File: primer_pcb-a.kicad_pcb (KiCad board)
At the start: 2 copper layers, 50 x 50 mm, 4 parts, among them J1 Pinheader - muški, J2 Pinheader - ženski, J3 Pinheader - ženski, J4 Pinheader - muški

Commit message: ds
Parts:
- added J5: Pinheader - ženski, Connector_PinSocket_2.54mm:PinSocket_1x01_P2.54mm_Horizontal, F.Cu at (109.0, 116.8)
- added J6: Pinheader - muški, Connector_PinHeader_2.54mm:PinHeader_1x01_P2.54mm_Horizontal, F.Cu at (147.4, 126.5)
- added J7: Pinheader - ženski, Connector_PinSocket_2.54mm:PinSocket_1x01_P2.54mm_Horizontal, F.Cu at (108.8, 123.6)
- added J8: Pinheader - ženski, Connector_PinSocket_2.54mm:PinSocket_1x01_P2.54mm_Horizontal, F.Cu at (107.5, 131.6)
- added Q2: BD910, Package_TO_SOT_THT:TO-220-3_Vertical, F.Cu at (125.1, 118.3)
- added Q3: BD909, Package_TO_SOT_THT:TO-220-3_Vertical, F.Cu at (125.1, 132.0)

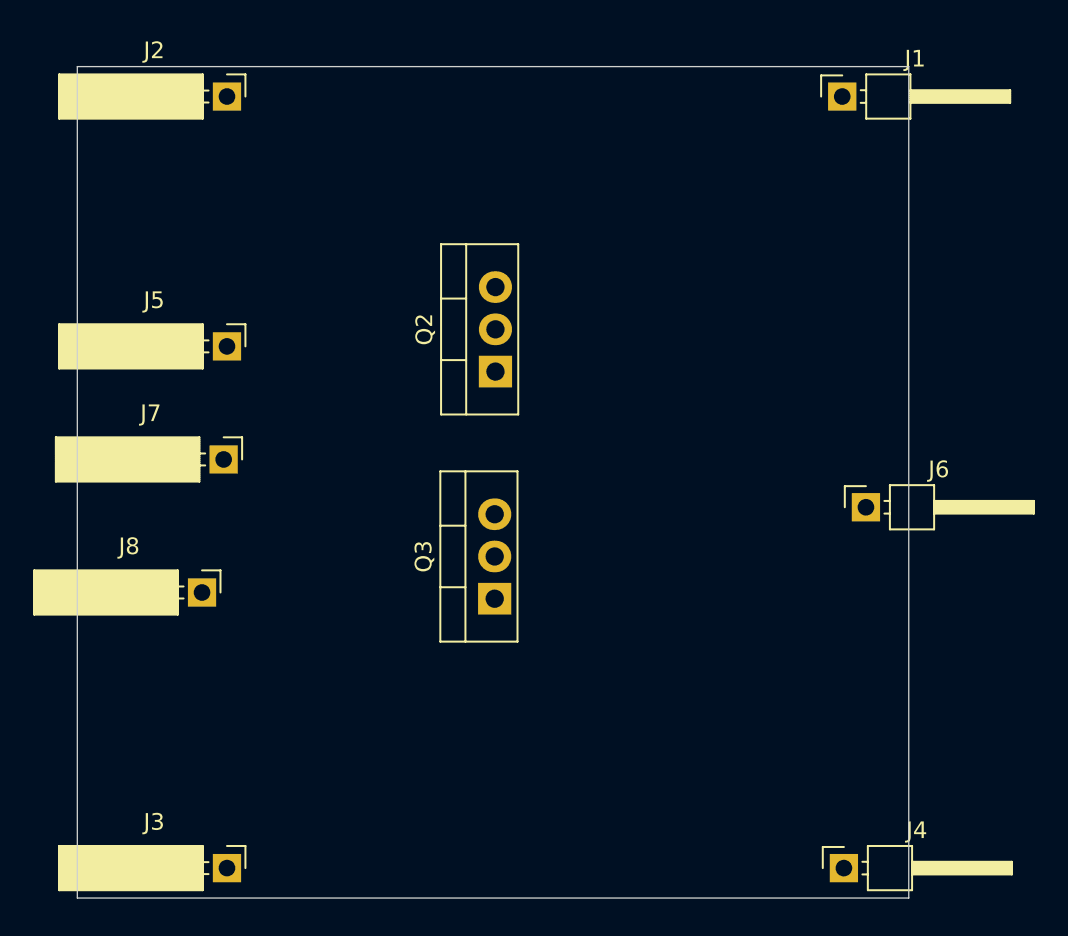
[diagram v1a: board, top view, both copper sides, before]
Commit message: New footprints, new connectors.
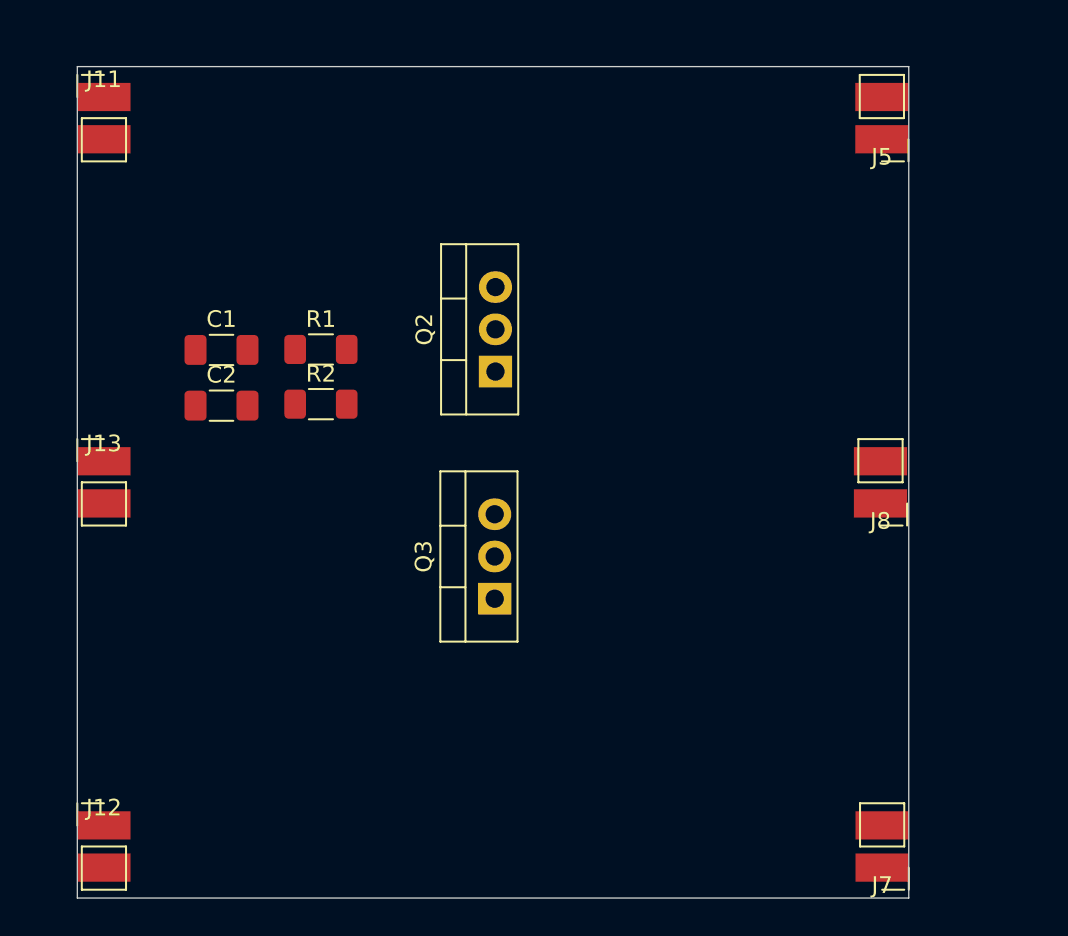
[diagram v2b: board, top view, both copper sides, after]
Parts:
- removed J1, J4, J6: Pinheader - muški, Connector_PinHeader_2.54mm:PinHeader_1x01_P2.54mm_Horizontal
- removed J2, J3: Pinheader - ženski, Connector_PinSocket_2.54mm:PinSocket_1x01_P2.54mm_Horizontal
- added C1: 1u, Capacitor_SMD:C_1206_3216Metric_Pad1.33x1.80mm_HandSolder, F.Cu at (108.7, 117.0)
- added C2: 1u, Capacitor_SMD:C_1206_3216Metric_Pad1.33x1.80mm_HandSolder, F.Cu at (108.7, 120.4)
- added J11: Pinheader - muški, primer_lib:PinHeader_1x02_P2.54mm_Polegnut, F.Cu at (101.6, 103.1)
- added J12: Pinheader - muški, primer_lib:PinHeader_1x02_P2.54mm_Polegnut, F.Cu at (101.6, 146.9)
- added J13: Pinheader - muški, primer_lib:PinHeader_1x02_P2.54mm_Polegnut, F.Cu at (101.6, 125.0)
- added R1: 1k, Resistor_SMD:R_1206_3216Metric_Pad1.30x1.75mm_HandSolder, F.Cu at (114.7, 117.0)
- added R2: 1k, Resistor_SMD:R_1206_3216Metric_Pad1.30x1.75mm_HandSolder, F.Cu at (114.7, 120.3)
- J5, J7, J8: value Pinheader - ženski -> Conn_01x02_Socket; footprint Connector_PinSocket_2.54mm:PinSocket_1x01_P2.54mm_Horizontal -> primer_lib:PinSocket_1x02_P2.54mm_Polegnut
- moved J7 45.9 mm to (148.4, 146.9), turned to 180 degrees
- moved J5 41.7 mm to (148.4, 103.1), turned to 180 degrees
- moved J8 41.3 mm to (148.3, 125.0), turned to 180 degrees
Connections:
- J5 pad 1: Net-(J5-Pin_1) -> VCC
- J7 pad 1: VCC -> GND
- J8 pad 1: GND -> Net-(J8-Pin_1)

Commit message: k
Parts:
- moved C2 26.6 mm to (134.6, 126.1)
- moved Q3 10.4 mm to (125.1, 121.6)
- moved Q2 9.23 mm to (124.8, 127.6), turned to -90 degrees
- moved R2 8.86 mm to (118.0, 128.5), turned to -90 degrees
- moved C1 6.39 mm to (109.3, 123.4)
- moved R1 4.92 mm to (117.9, 120.7), turned to -90 degrees
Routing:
- net Net-(Q2-B): track 0.00 -> 26.8 mm
- net Net-(Q2-E): track 0.00 -> 25.6 mm
- net Net-(J8-Pin_1): track 0.00 -> 12.2 mm
- net GND: track 0.00 -> 9.66 mm
- net Net-(J13-Pin_1): track 0.00 -> 6.27 mm
- added copper zone on F.Cu, net GND
- added copper zone on F.Cu, net VCC

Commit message: Added mounting holes.
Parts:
- added H1: MountingHole, MountingHole:MountingHole_3.2mm_M3, F.Cu at (125.0, 105.0)
- added H2: MountingHole, MountingHole:MountingHole_3.2mm_M3, F.Cu at (125.0, 145.0)
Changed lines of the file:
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@@
 		)
+	)
+	(footprint "MountingHole:MountingHole_3.2mm_M3"
+		(layer "F.Cu")
+		(at 125 145)
+		(descr "Mounting Hole 3.2mm, no annular, M3")
+		(tags "mounting hole 3.2mm no annular m3")
+		(property "Reference" "H2"
+			(at 0 -4.2 0)
+			(layer "F.SilkS")
+			(effects
+				(font
+					(size 1 1)
+					(thickness 0.15)
+				)
+			)
+		)
+		(property "Value" "MountingHole"
+			(at 0 4.2 0)
+			(layer "F.Fab")
+			(effects
+				(font
+					(size 1 1)
+					(thickness 0.15)
+				)
+			)
+		)
+		(property "Datasheet" ""
+			(at 0 0 0)
+			(unlocked yes)
+			(layer "F.Fab")
+			(hide yes)
+			(effects
+				(font
+					(size 1.27 1.27)
+					(thickness 0.15)
+				)
+			)
+		)
+		(property "Description" "Mounting Hole without connection"
+			(at 0 0 0)
+			(unlocked yes)
+			(layer "F.Fab")
+			(hide yes)
+			(effects
+				(font
+					(size 1.27 1.27)
+					(thickness 0.15)
+				)
+			)
+		)
+		(property ki_fp_filters "MountingHole*")
+		(sheetname "/")
+		(sheetfile "primer_pcb-a.kicad_sch")
+		(attr exclude_from_pos_files exclude_from_bom)
+		(fp_circle
+			(center 0 0)
+			(end 3.2 0)
+			(stroke
+				(width 0.15)
+				(type solid)
+			)
+			(fill no)
+			(layer "Cmts.User")
+		)
+		(fp_circle
+			(center 0 0)
+			(end 3.45 0)
+			(stroke
+				(width 0.05)
+				(type solid)
+			)
+			(fill no)
+			(layer "F.CrtYd")
+		)
+		(fp_text user "${REFERENCE}"
+			(at 0 0 0)
+			(layer "F.Fab")
+			(effects
+				(font
+					(size 1 1)
+					(thickness 0.15)
+				)
+			)
+		)
+		(pad "" np_thru_hole circle
+			(at 0 0)
+			(size 3.2 3.2)
+			(drill 3.2)
+			(layers "*.Cu" "*.Mask")
+		)
+		(embedded_fonts no)
 	)
 	(footprint "Resistor_SMD:R_1206_3216Metric_Pad1.30x1.75mm_HandSolder"
@@
 		)
 	)
+	(footprint "MountingHole:MountingHole_3.2mm_M3"
+		(layer "F.Cu")
+		(at 125 105)
+		(descr "Mounting Hole 3.2mm, no annular, M3")
+		(tags "mounting hole 3.2mm no annular m3")
+		(property "Reference" "H1"
+			(at 0 -4.2 0)
+			(layer "F.SilkS")
+			(effects
+				(font
+					(size 1 1)
+					(thickness 0.15)
+				)
+			)
+		)
+		(property "Value" "MountingHole"
+			(at 0 4.2 0)
+			(layer "F.Fab")
+			(effects
+				(font
+					(size 1 1)
+					(thickness 0.15)
+				)
+			)
+		)
+		(property "Datasheet" ""
+			(at 0 0 0)
+			(unlocked yes)
+			(layer "F.Fab")
+			(hide yes)
+			(effects
+				(font
+					(size 1.27 1.27)
+					(thickness 0.15)
+				)
+			)
+		)
+		(property "Description" "Mounting Hole without connection"
+			(at 0 0 0)
+			(unlocked yes)
+			(layer "F.Fab")
+			(hide yes)
+			(effects
+				(font
+					(size 1.27 1.27)
+					(thickness 0.15)
+				)
+			)
+		)
+		(property ki_fp_filters "MountingHole*")
+		(sheetname "/")
+		(sheetfile "primer_pcb-a.kicad_sch")
+		(attr exclude_from_pos_files exclude_from_bom)
+		(fp_circle
+			(center 0 0)
+			(end 3.2 0)
+			(stroke
+				(width 0.15)
+				(type solid)
+			)
+			(fill no)
+			(layer "Cmts.User")
+		)
+		(fp_circle
+			(center 0 0)
+			(end 3.45 0)
+			(stroke
+				(width 0.05)
+				(type solid)
+			)
+			(fill no)
+			(layer "F.CrtYd")
+		)
+		(fp_text user "${REFERENCE}"
+			(at 0 0 0)
+			(layer "F.Fab")
+			(effects
+				(font
+					(size 1 1)
+					(thickness 0.15)
+				)
+			)
+		)
+		(pad "" np_thru_hole circle
+			(at 0 0)
+			(size 3.2 3.2)
+			(drill 3.2)
+			(layers "*.Cu" "*.Mask")
+		)
+		(embedded_fonts no)
+	)
 	(footprint "primer_lib:PinHeader_1x02_P2.54mm_Polegnut"

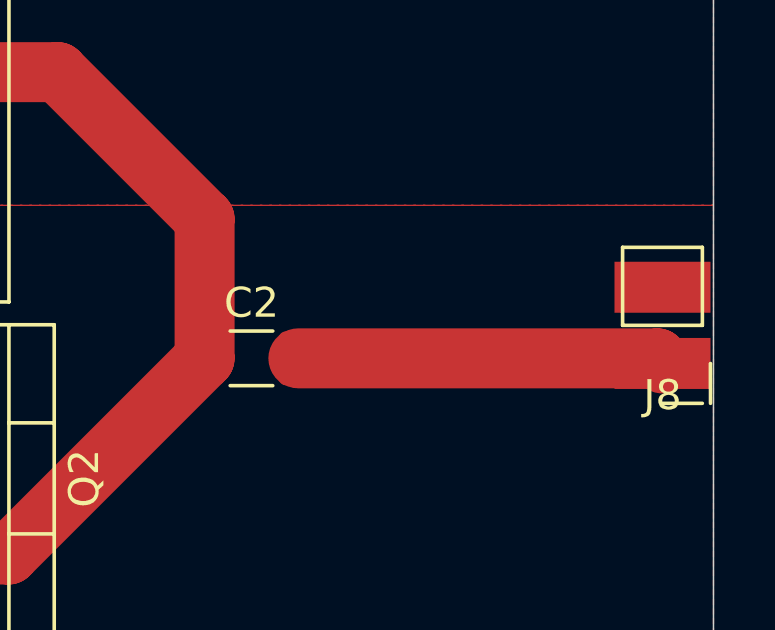
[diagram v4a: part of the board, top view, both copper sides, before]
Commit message: Updated pins
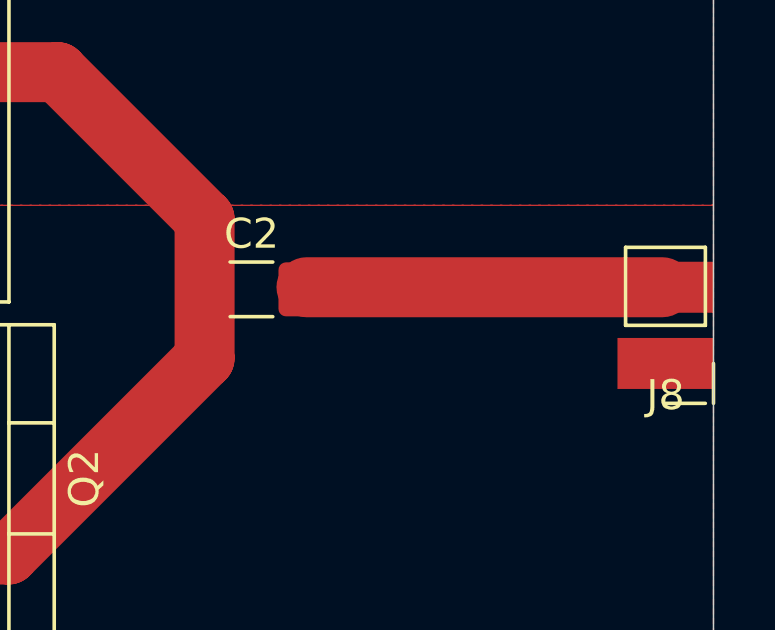
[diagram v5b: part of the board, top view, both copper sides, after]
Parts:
- moved C2 2.30 mm to (134.6, 123.8)
- moved J8 0.10 mm to (148.4, 125.0)
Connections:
- C2 pad 2: Net-(J8-Pin_1) -> Net-(J8-Pin_2)
- J8 pad 1: Net-(J8-Pin_1) -> GND
- J8 pad 2: GND -> Net-(J8-Pin_2)
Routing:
- net Net-(J8-Pin_1): track 12.2 -> 0.00 mm
- net Net-(J8-Pin_2): track 0.00 -> 11.9 mm
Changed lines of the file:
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@@
 	(net 1 "VCC")
 	(net 2 "GND")
-	(net 3 "Net-(J8-Pin_1)")
+	(net 3 "Net-(J8-Pin_2)")
 	(net 4 "Net-(Q2-B)")
 	(net 5 "Net-(Q2-E)")
@@
 	(footprint "Capacitor_SMD:C_1206_3216Metric_Pad1.33x1.80mm_HandSolder"
 		(layer "F.Cu")
-		(at 134.6 126.1)
+		(at 134.6 123.8)
 		(descr "Capacitor SMD 1206 (3216 Metric), square (rectangular) end terminal, IPC_7351 nominal with elongated pad for handsoldering. (Body size source: IPC-SM-782 page 76, https://www.pcb-3d.com/wordpress/wp-content/uploads/ipc-sm-782a_amendment_1_and_2.pdf), generated with kicad-footprint-generator")
 		(tags "capacitor handsolder")
@@
 			(layers "F.Cu" "F.Mask" "F.Paste")
 			(roundrect_rratio 0.188679)
-			(net 3 "Net-(J8-Pin_1)")
+			(net 3 "Net-(J8-Pin_2)")
 			(pintype "passive")
 		)
@@
 	(footprint "primer_lib:PinSocket_1x02_P2.54mm_Polegnut"
 		(layer "F.Cu")
-		(at 148.3 125 180)
+		(at 148.4 125 180)
 		(descr "Through hole straight pin header, 1x02, 2.54mm pitch, single row")
 		(tags "Through hole pin header THT 1x02 2.54mm single row")
@@
 			(size 3.2 1.7)
 			(layers "F.Cu" "F.Mask" "F.Paste")
-			(net 3 "Net-(J8-Pin_1)")
+			(net 2 "GND")
 			(pinfunction "Pin_1")
 			(pintype "passive")
@@
 			(size 3.2 1.7)
 			(layers "F.Cu" "F.Mask" "F.Paste")
-			(net 2 "GND")
+			(net 3 "Net-(J8-Pin_2)")
 			(pinfunction "Pin_2")
 			(pintype "passive")
@@
 	)
 	(segment
-		(start 148.13 126.1)
-		(end 148.3 126.27)
-		(width 2)
-		(layer "F.Cu")
-		(net 3)
-	)
-	(segment
-		(start 136.1625 126.1)
-		(end 148.13 126.1)
+		(start 148.3 123.73)
+		(end 136.4325 123.73)
 		(width 2)
 		(layer "F.Cu")
@@
 		(priority 1)
 		(connect_pads yes
-			(clearance 2)
+			(clearance 1)
 		)
 		(min_thickness 0.25)
@@
 		(hatch edge 0.5)
 		(connect_pads yes
-			(clearance 1.5)
+			(clearance 1)
 		)
 		(min_thickness 0.25)
